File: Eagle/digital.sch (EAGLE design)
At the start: 31 parts, among them J1 USB-B

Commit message: Finished digital board
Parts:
- added C12, C14, C18, C19: 0.1uF, resistor:C-EU050-025X075
- added C13, C20, C21: 0.01uF, resistor:C-EU050-025X075
- added C15: 47uF, resistor:CPOL-USE5-8.5
- added IC3: MAX6341N, EEG:MAX6341N
- added L1: BL02RN1, inductors:BL02RN1
- added LED1: (no value), led:LED3MM
- added R3: 200k, resistor:R-US_0204/2V
- added R4, R5: 20k, resistor:R-US_0204/2V
- added R6: (no value), resistor:R-TRIMM3296W
- added U$3: ROL-0505S, modEEG:ROL-0505S
- renumbered VREF to VCOM
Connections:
- removed net VDD: AMP0.3, AMP1.3, AMP2.3, AMP3.3, AMP4.3, AMP5.3, AMP6.3, AMP7.3
- new net +5V/2: C10.+, C11.1, C3.1, C4.1, C5.1, CN1.PWR, D1.C, U$1.VDD$1, U$1.VDD$2, U$2.VCC, U$3.IN+
- new net DGND: C1.1, C10.-, C11.2, C2.1, C4.2, C5.2, CN1.GND, D1.A, J1.GND, U$1.VSS$1, U$1.VSS$2, U$2.GND, U$3.IN-
- new net N$27: R4.2, R6.A
- new net N$28: LED1.A, R3.1
- new net VCOM: AMP0.2, AMP1.2, AMP2.2, AMP3.2, AMP4.2, AMP5.2, AMP6.2, AMP7.2, C18.2, C19.1, C8.1, C9.1, IC2B.-IN, IC2B.OUT, R1.E, VCOM.P
- net +5V: now also C13.1, C14.1, C15.+, C18.1, IC3.+VIN, L1.1; no longer C3.1, C4.1, C5.1, U$1.VDD$1, U$1.VDD$2, U$2.VCC
- net GND: now also C12.2, C13.2, C14.2, C15.-, C19.2, C20.2, C21.2, IC3.GND, LED1.C, R4.1, U$3.OUT-; no longer C1.1, C2.1, C4.2, C5.2, J1.GND, U$2.GND
- net N$23: now also R5.1, R6.E; no longer C10.+, C11.1, CN1.PWR, D1.C
- net N$24: now also C20.1, IC2B.+IN, R6.S; no longer C10.-, C11.2, CN1.GND, D1.A
- net N$26: now also C12.1, L1.2, R3.2, U$3.OUT+; no longer U$1.VSS$1, U$1.VSS$2
- net VREF: now also AMP0.3, AMP1.3, AMP2.3, AMP3.3, AMP4.3, AMP5.3, AMP6.3, AMP7.3, C21.1, IC3.VOUT, R5.2; no longer AMP0.2, AMP1.2, AMP2.2, AMP3.2, AMP4.2, AMP5.2, AMP6.2, AMP7.2, C8.1, C9.1, R1.E, VCOM.P
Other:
- note added: "VCOM"
- note removed: "VREF"
- moved on the sheet: C10, C11, CN1, D1

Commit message: Finished up chanes to DB25
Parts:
- removed AMP0, AMP1, AMP2, AMP3, AMP4, AMP5, AMP6, AMP7: 0446200002, con-molex:0446200002
- removed C18, C19, C8, C9: 0.1uF, resistor:C-EU050-025X075
- removed C20, C21: 0.01uF, resistor:C-EU050-025X075
- removed C6, C7: 1nF, resistor:C-EU050-025X075
- removed IC2: (no value), BURR:TLC277P
- removed IC3: MAX6341N, EEG:MAX6341N
- removed R1: (no value), pot:TRIM_US-B64Y
- removed R2: 200k, resistor:R-US_0204/7
- removed R4, R5: 20k, resistor:R-US_0204/2V
- removed R6: (no value), resistor:R-TRIMM3296W
- removed RLD_COM, RLD_OUT, VCOM: (no value), wirepad:2,15/1,0
- added JP1: (no value), jumper:JP1Q
- added X1: (no value), con-subd:M25HS
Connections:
- removed net N$21: C7.1, IC2A.OUT, R2.2
- removed net N$22: C6.1, C7.2, R2.1, RLD_OUT.P
- removed net N$23: R5.1, R6.E
- removed net N$24: C20.1, IC2B.+IN, R6.S
- removed net N$27: R4.2, R6.A
- removed net RLD: AMP0.1, AMP1.1, AMP2.1, AMP3.1, AMP4.1, AMP5.1, AMP6.1, AMP7.1, C6.2, IC2A.-IN, RLD_COM.P
- removed net VCOM: AMP0.2, AMP1.2, AMP2.2, AMP3.2, AMP4.2, AMP5.2, AMP6.2, AMP7.2, C18.2, C19.1, C8.1, C9.1, IC2B.-IN, IC2B.OUT, R1.E, VCOM.P
- removed net VREF: AMP0.3, AMP1.3, AMP2.3, AMP3.3, AMP4.3, AMP5.3, AMP6.3, AMP7.3, C21.1, IC3.VOUT, R5.2
- new net CNV: U$1.RC6, X1-19.M
- new net RD0: U$1.RD0, X1-8.M
- new net RD1: U$1.RD1, X1-20.M
- new net SCK: U$1.RC7, X1-7.M
- net +5V: now also X1-17.M; no longer AMP0.4, AMP1.4, AMP2.4, AMP3.4, AMP4.4, AMP5.4, AMP6.4, AMP7.4, C18.1, C8.2, IC2PWR.VCC, IC3.+VIN
- net +5V/2: now also JP1.2; no longer U$2.VCC
- net GND: now also X1-1.M, X1-14.M, X1-16.M, X1-18.M, X1-4.M, X1-6.M; no longer AMP0.8, AMP0.S1, AMP0.S2, AMP1.8, AMP1.S1, AMP1.S2, AMP2.8, AMP2.S1, AMP2.S2, AMP3.8, AMP3.S1, AMP3.S2, AMP4.8, AMP4.S1, AMP4.S2, AMP5.8, AMP5.S1, AMP5.S2, AMP6.8, AMP6.S1, AMP6.S2, AMP7.8, AMP7.S1, AMP7.S2, C19.2, C20.2, C21.2, C9.2, IC2PWR.GND, IC3.GND, R1.A, R4.1
- net N$10: now also JP1.1, U$2.VCC; no longer IC2A.+IN, R1.S
- net N$11: now also U$1.RB4, X1-13.M; no longer AMP7.6, U$1.RD7
- net N$12: now also U$1.RB3, X1-25.M; no longer AMP6.6, U$1.RD6
- net N$13: now also U$1.RB2, X1-12.M; no longer AMP5.6, U$1.RD5
- net N$14: now also U$1.RB1, X1-24.M; no longer AMP4.6, U$1.RD4
- net N$15: now also U$1.RD7, X1-11.M; no longer AMP3.6, U$1.RD3
- net N$16: now also U$1.RD6, X1-23.M; no longer AMP2.6, U$1.RD2
- net N$17: now also U$1.RD5, X1-10.M; no longer AMP1.6, U$1.RD1
- net N$18: now also U$1.RD4, X1-22.M; no longer AMP0.6, U$1.RD0
- net N$19: now also U$1.RD3, X1-9.M; no longer AMP0.5, AMP1.5, AMP2.5, AMP3.5, AMP4.5, AMP5.5, AMP6.5, AMP7.5, U$1.RC6
- net N$20: now also U$1.RD2, X1-21.M; no longer AMP0.7, AMP1.7, AMP2.7, AMP3.7, AMP4.7, AMP5.7, AMP6.7, AMP7.7, U$1.RC7
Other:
- note removed: "RLD"
- note removed: "VCOM"

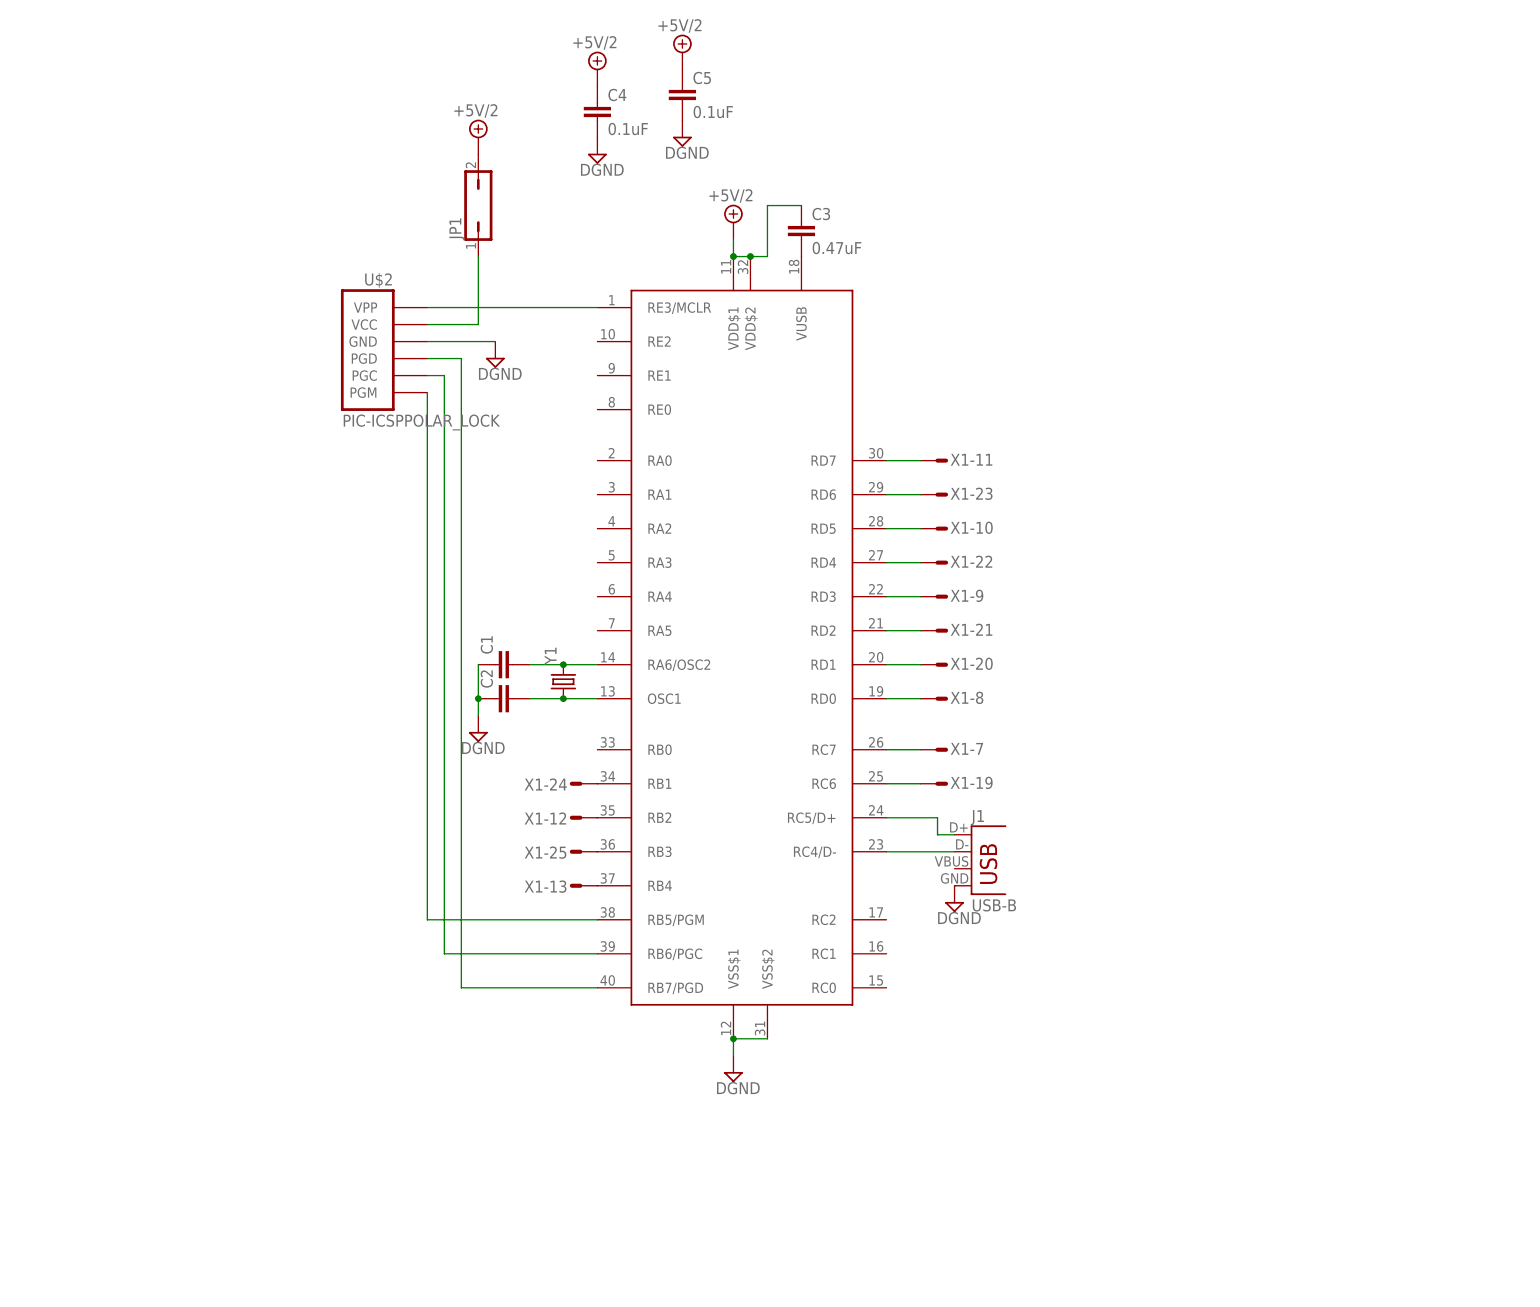
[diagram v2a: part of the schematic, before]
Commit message: Added optoisolators
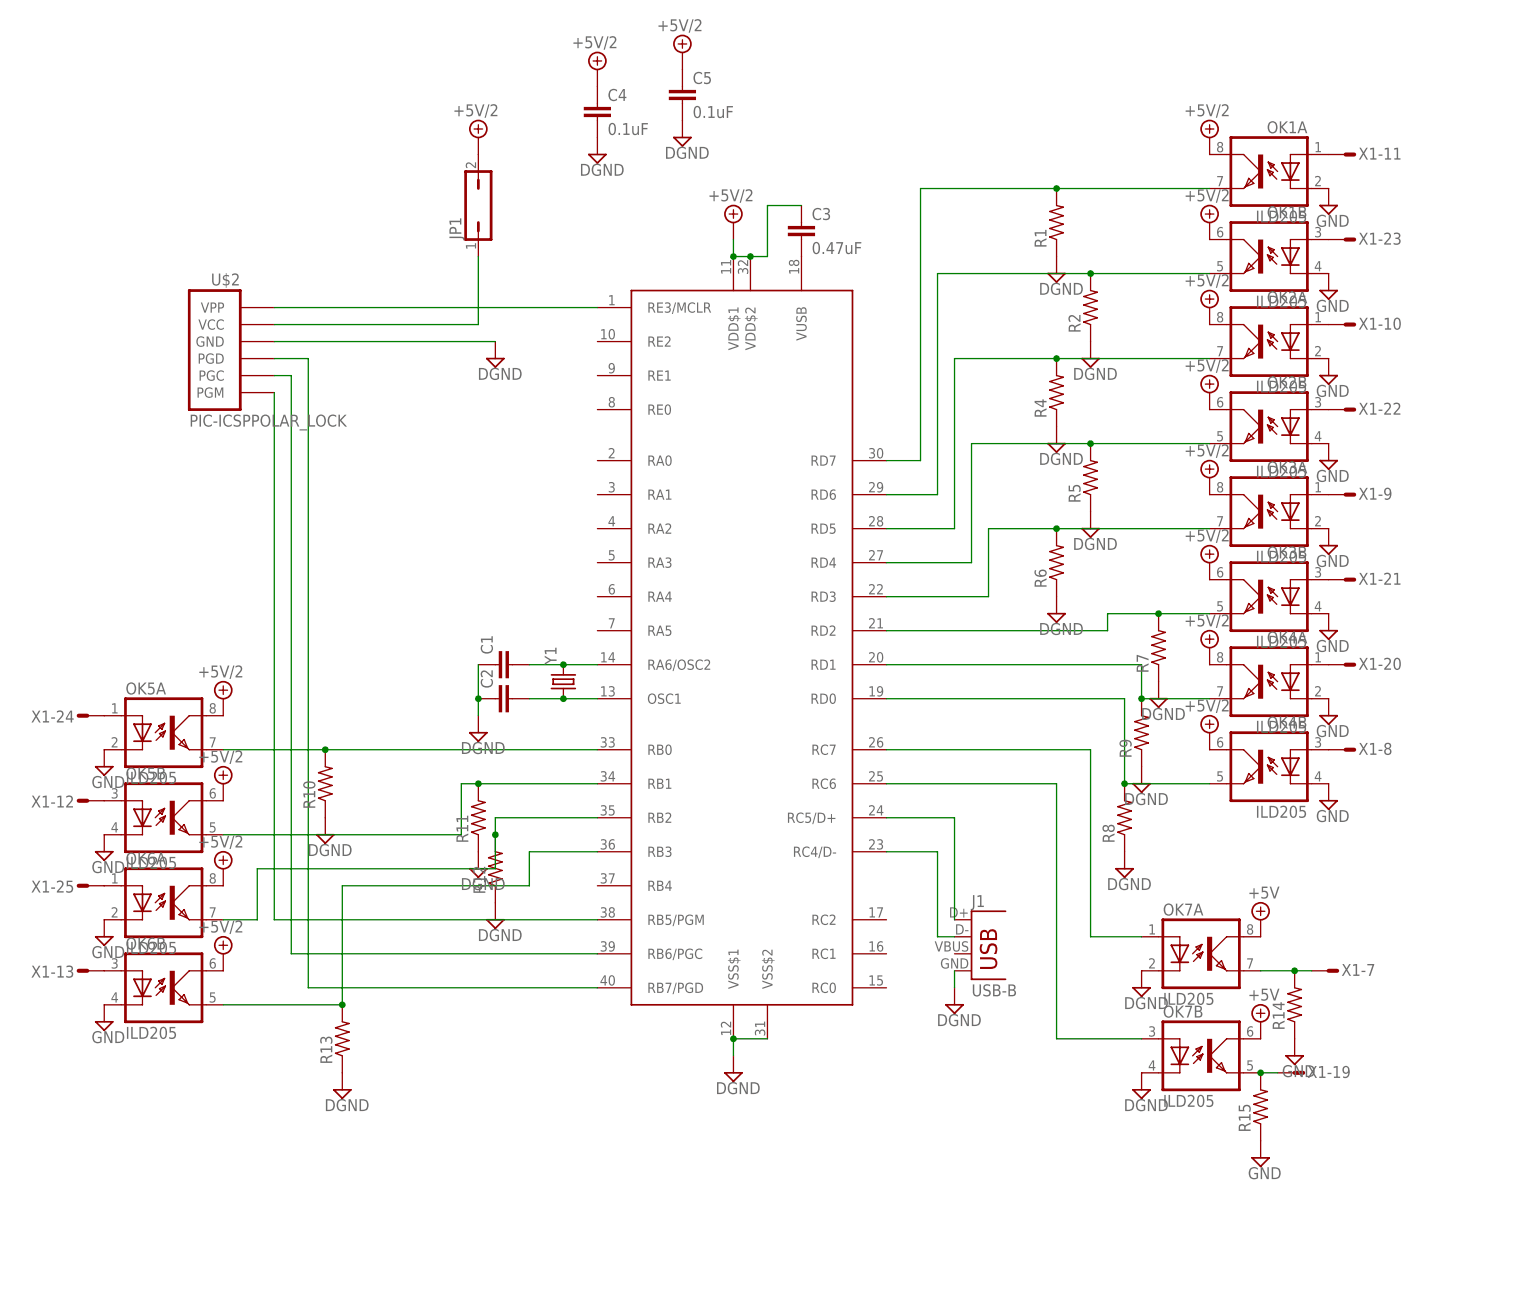
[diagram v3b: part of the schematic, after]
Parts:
- added OK1, OK2, OK3, OK4, OK5, OK6, OK7: ILD205, optocoupler:ILD205
- added R1, R10, R11, R12, R13, R14, R15, R2, R4, R5, R6, R7, R8, R9: (no value), resistor:R-US_0204/2V
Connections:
- removed net CNV: U$1.RC6, X1-19.M
- removed net RD0: U$1.RD0, X1-8.M
- removed net RD1: U$1.RD1, X1-20.M
- removed net SCK: U$1.RC7, X1-7.M
- new net N$21: OK5B.A, X1-12.M
- new net N$22: OK6A.A, X1-25.M
- new net N$23: OK6B.A, X1-13.M
- new net N$24: OK1B.EMIT, R2.2, U$1.RD6
- new net N$25: OK2A.EMIT, R4.2, U$1.RD5
- new net N$27: OK2B.EMIT, R5.2, U$1.RD4
- new net N$29: OK3A.EMIT, R6.2, U$1.RD3
- new net N$30: OK3B.EMIT, R7.2, U$1.RD2
- new net N$31: OK4A.EMIT, R9.2, U$1.RD1
- new net N$32: OK4B.EMIT, R8.2, U$1.RD0
- new net N$33: OK5A.EMIT, R10.2, U$1.RB0
- new net N$34: OK5B.EMIT, R11.2, U$1.RB1
- new net N$35: OK6A.EMIT, R12.2, U$1.RB2
- new net N$36: OK6B.EMIT, R13.2, U$1.RB3
- new net N$37: OK7A.EMIT, R14.2, X1-7.M
- new net N$38: OK7B.EMIT, R15.2, X1-19.M
- new net N$39: OK7A.A, U$1.RC7
- new net N$40: OK7B.A, U$1.RC6
- net +5V: now also OK7A.COL, OK7B.COL
- net +5V/2: now also OK1A.COL, OK1B.COL, OK2A.COL, OK2B.COL, OK3A.COL, OK3B.COL, OK4A.COL, OK4B.COL, OK5A.COL, OK5B.COL, OK6A.COL, OK6B.COL
- net DGND: now also OK7A.C, OK7B.C, R1.1, R10.1, R11.1, R12.1, R13.1, R2.1, R4.1, R5.1, R6.1, R7.1, R8.1, R9.1
- net GND: now also OK1A.C, OK1B.C, OK2A.C, OK2B.C, OK3A.C, OK3B.C, OK4A.C, OK4B.C, OK5A.C, OK5B.C, OK6A.C, OK6B.C, R14.1, R15.1
- net N$11: now also OK1A.A, X1-11.M; no longer U$1.RB4, X1-13.M
- net N$12: now also OK1B.A, X1-23.M; no longer U$1.RB3, X1-25.M
- net N$13: now also OK2A.A, X1-10.M; no longer U$1.RB2, X1-12.M
- net N$14: now also OK2B.A, X1-22.M; no longer U$1.RB1, X1-24.M
- net N$15: now also OK1A.EMIT, R1.2; no longer X1-11.M
- net N$16: now also OK3A.A, X1-9.M; no longer U$1.RD6, X1-23.M
- net N$17: now also OK3B.A, X1-21.M; no longer U$1.RD5, X1-10.M
- net N$18: now also OK4A.A, X1-20.M; no longer U$1.RD4, X1-22.M
- net N$19: now also OK4B.A, X1-8.M; no longer U$1.RD3, X1-9.M
- net N$20: now also OK5A.A, X1-24.M; no longer U$1.RD2, X1-21.M
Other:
- moved on the sheet: J1, U$2, X1-10, X1-11, X1-12, X1-13, X1-19, X1-20, X1-21, X1-22, X1-23, X1-24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
